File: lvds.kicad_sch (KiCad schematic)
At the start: 108 parts, among them J3 Conn_FFC_Amphenol_62684-40210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, Q2 PJE138K, Q3 SSM3J332R, Q4 PJE138K, Q5 SSM3J332R, Q6 PJE138K, Q7 SSM3J332R, U4 TPS65150PWP, U5 MPQ7235GQBE, U6 TLV76701_WSON6

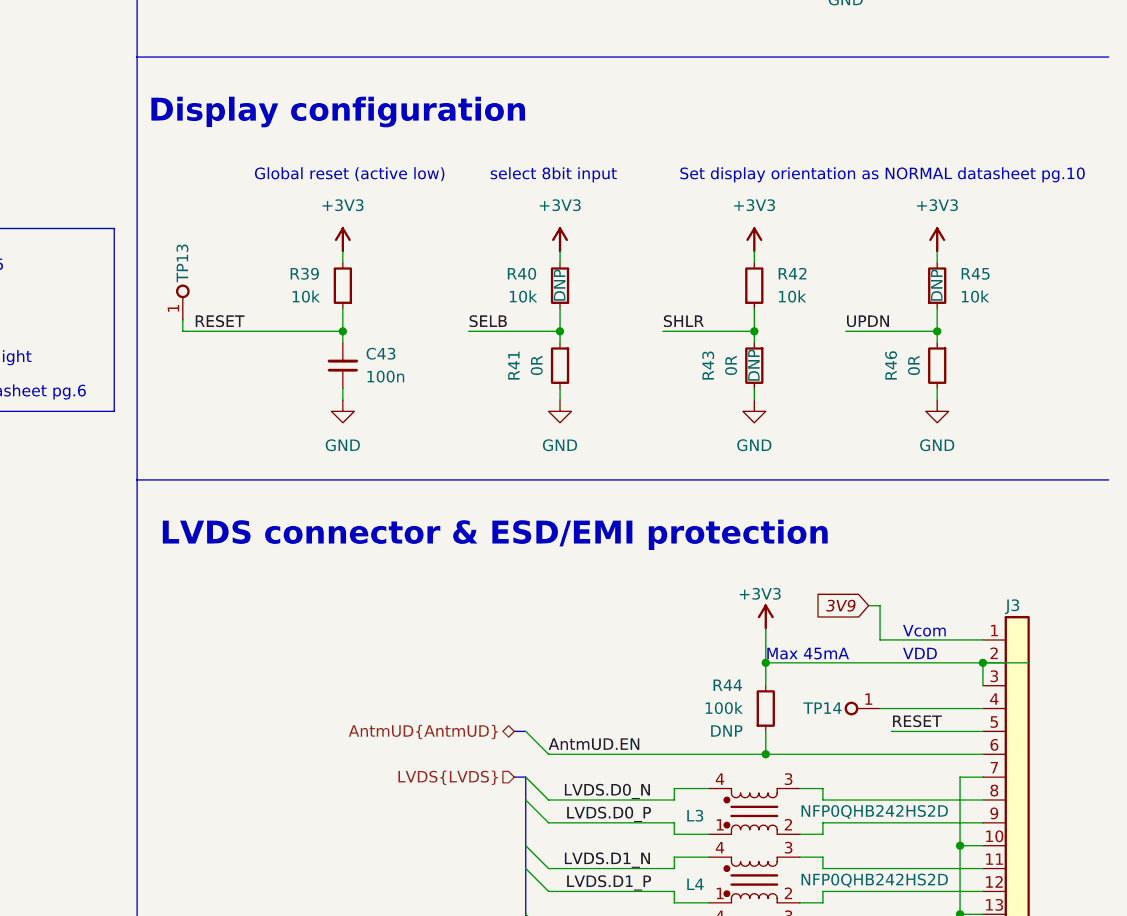
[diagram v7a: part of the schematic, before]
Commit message: [#54932] Connect display to ~{RST}; Connect 1V8 LDO to EN; Fix bus definition
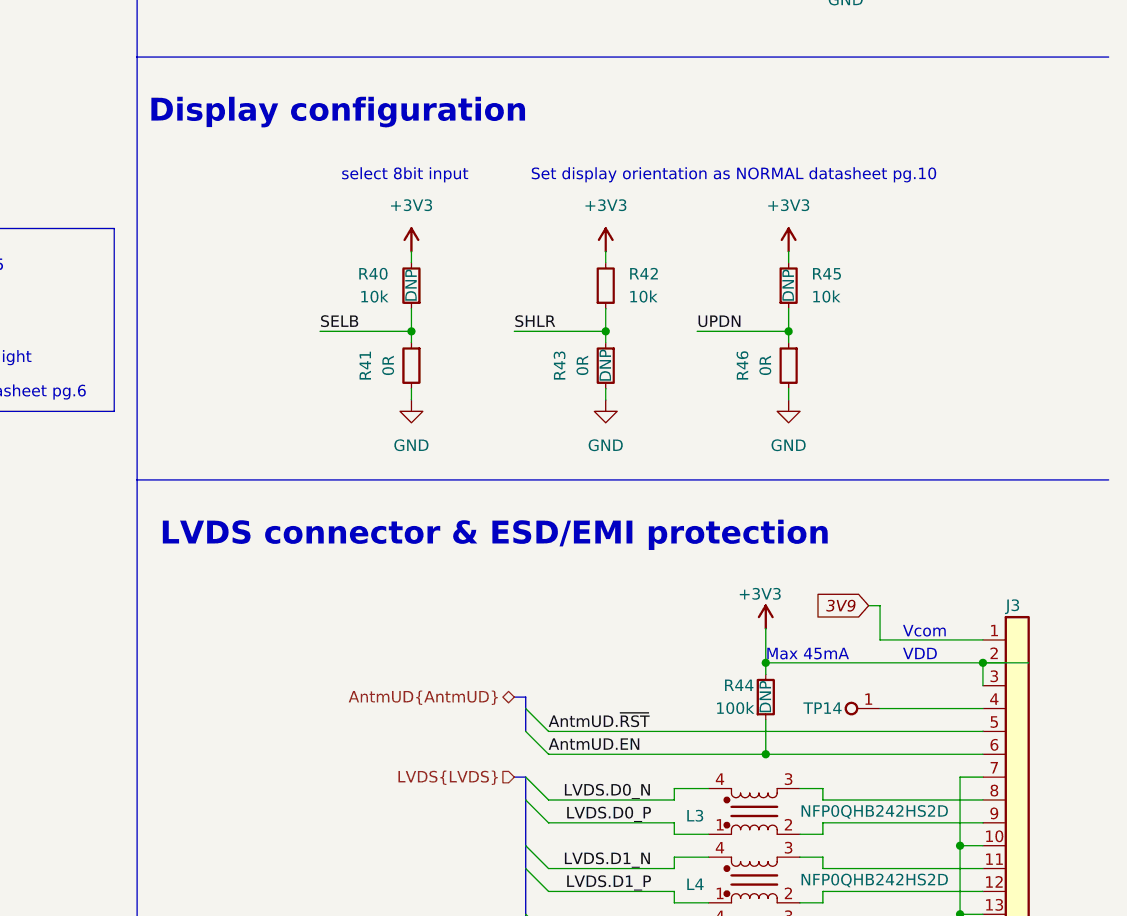
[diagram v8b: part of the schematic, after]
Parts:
- removed C43: C_100n_0402, antmicro-footprints:C_0402_1005Metric, symbol antmicroCapacitors0402:C_100n_0402
- removed R39: R_10k_0402, antmicro-footprints:R_0402_1005Metric, symbol antmicroResistors0402:R_10k_0402
- removed TP13: TP_0.75mm_SMD, antmicro-footprints:TP_SMD_0.75mm, symbol antmicroTestPoints:TP_0.75mm_SMD
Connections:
- net RESET renamed AntmUD.~{RST}
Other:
- note removed: "Global reset (active low)"
- moved on the sheet: R40, R41, R42, R43, R44, R45, R46
